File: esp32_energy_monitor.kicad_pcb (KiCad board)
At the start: 4 copper layers, 54 x 33.7 mm, 73 parts, among them IC1 CP2102N-A01-GQFN28, IC2 TPS63031DSKT, IC3 MCP73830T-2AAI_MYY, J1 USB, J2 Conn_01x03, J3 Conn_01x02, J4 Conn_01x02, J5 Conn_01x02, J6 Conn_01x04, J7 Conn_01x04, Q1 SS8050-G, Q2 SS8050-G, Q3 CSD16406Q3, Q4 CSD16406Q3, Q5 SS8050-G, SW1 SW_Push, SW2 SW_Push, U1 DRV8833PWPR, U2 BQ29700DSET

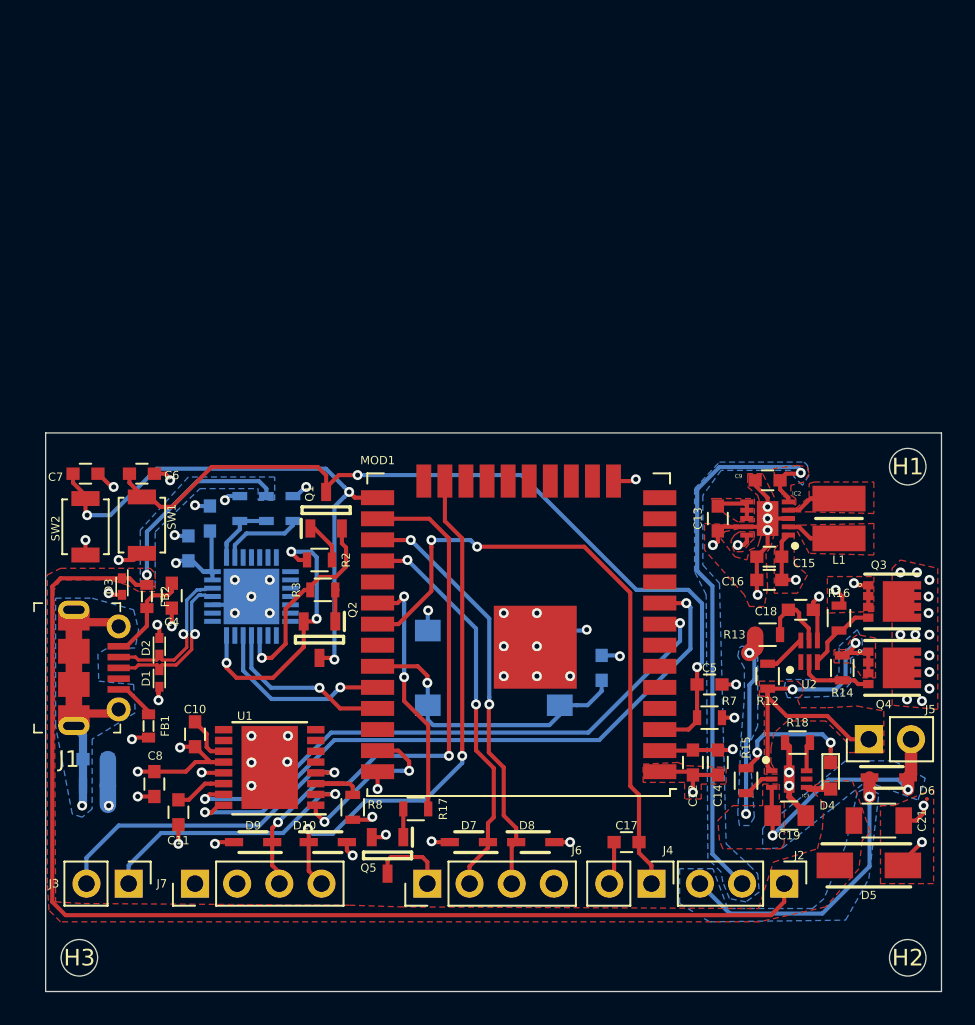
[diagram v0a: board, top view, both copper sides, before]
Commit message: Added the ADS1115IDGSR ADC circuit with the signal conditioning to current sensor SCT-013-020 (30A).
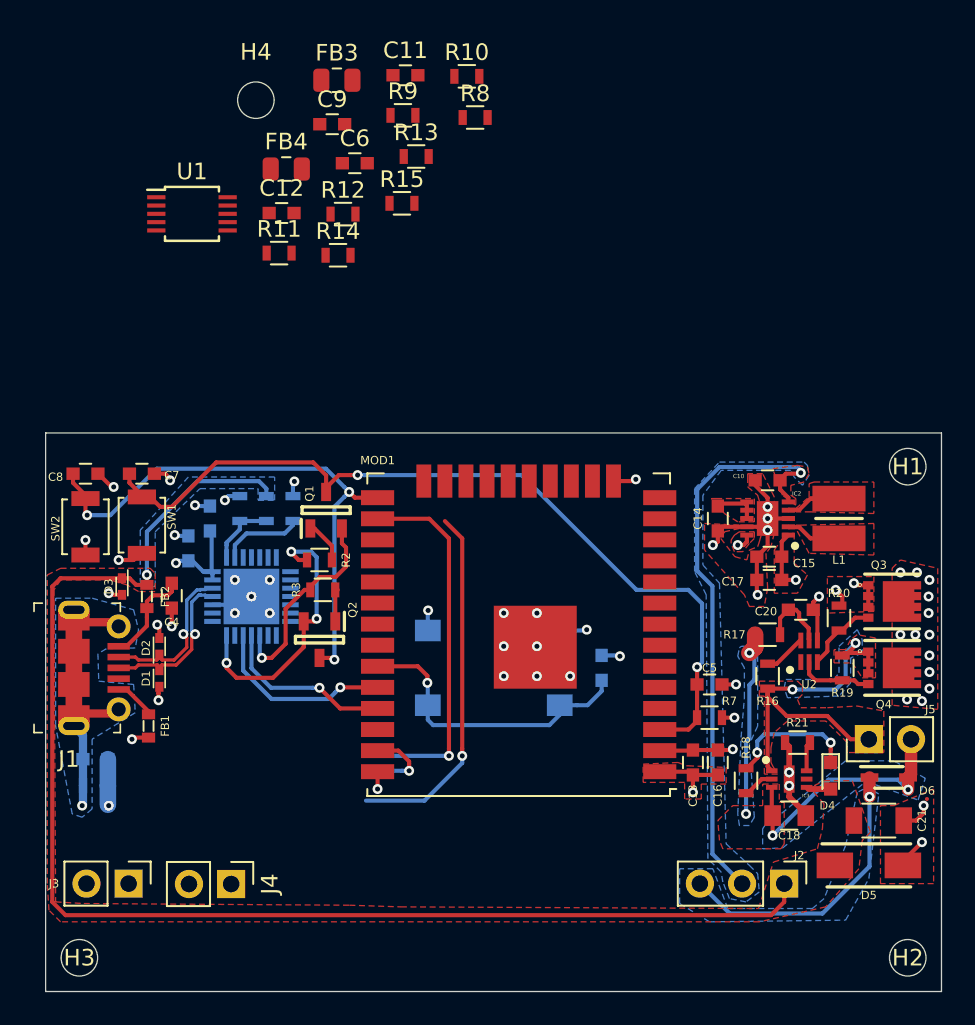
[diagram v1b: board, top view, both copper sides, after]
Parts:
- removed the C10 at (124.0, 91.5)
- removed the C17 at (150.0, 98.0)
- removed the C8 at (121.5, 94.5)
- removed D10, D7, D8, D9: PESD3V3L1BA,115, SamacSys_Parts:SOD2512X110N
- removed J6, J7: Conn_01x04, Pin_Headers:Pin_Header_Straight_1x04_Pitch2.54mm
- removed Q5: SS8050-G, SamacSys_Parts:SOT95P240X115-3N
- removed the R17 at (137.3, 96.0)
- added C12: 1uF, Capacitors_SMD:C_0603, F.Cu at (129.2, 60.1)
- added C6: 10uF ou 100uF, Capacitors_SMD:C_0603, F.Cu at (133.6, 57.1)
- added C9: 10uF ou 100uF, Capacitors_SMD:C_0603, F.Cu at (132.3, 54.7)
- added FB3: MMZ2012Y152BT000, Inductor_SMD:L_0805_2012Metric, F.Cu at (132.5, 52.1)
- added FB4: MMZ2012Y152BT000, Inductor_SMD:L_0805_2012Metric, F.Cu at (129.5, 57.4)
- added H4: M2Hole, Mounting_Holes:MountingHole_2.2mm_M2_DIN965, F.Cu at (127.7, 53.3)
- added R10: 100K/1%, Resistors_SMD:R_0603, F.Cu at (140.4, 51.9)
- added R11: 100K/1%, Resistors_SMD:R_0603, F.Cu at (129.1, 62.5)
- added R12: 10k, Resistors_SMD:R_0603, F.Cu at (132.9, 60.2)
- added R13: 10k, Resistors_SMD:R_0603, F.Cu at (137.3, 56.7)
- added R14: 10k, Resistors_SMD:R_0603, F.Cu at (132.6, 62.6)
- added R15: 10k, Resistors_SMD:R_0603, F.Cu at (136.5, 59.5)
- added R9: 100K/1%, Resistors_SMD:R_0603, F.Cu at (136.5, 54.2)
- C11: value 2.2uF -> 1uF
- J1: value USB -> USB_OTG
- R8: value 0.2R -> 100K/1%
- U1: value DRV8833PWPR -> ADS1115IDGS; footprint Housings_SSOP:HTSSOP-16-1EP_4.4x5mm_Pitch0.65mm -> Package_SO:TSSOP-10_3x3mm_P0.5mm
- moved C11 46.5 mm to (136.7, 51.8), turned to 0 degrees
- moved R8 42.2 mm to (140.9, 54.3), turned to 0 degrees
- moved U1 33.7 mm to (123.8, 60.1), turned to 0 degrees
- moved J4 25.3 mm to (126.2, 100.5)
- renumbered C9 to C10, C12 to C13, C13 to C14, C14 to C16, C16 to C17, C19 to C18, C20 to C19, C18 to C20, C6 to C7, C7 to C8, R12 to R16, R13 to R17, R15 to R18, R14 to R19, R16 to R20, R18 to R21
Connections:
- C11 pad 1: Net-(C11-Pad1) -> GNDD
- C11 pad 2: GND -> +3.3VADC
- IC1 pad 1: Net-(IC1-Pad1) -> (no net)
- IC1 pad 10: Net-(IC1-Pad10) -> (no net)
- IC1 pad 11: Net-(IC1-Pad11) -> (no net)
- IC1 pad 12: Net-(IC1-Pad12) -> (no net)
- IC1 pad 13: Net-(IC1-Pad13) -> (no net)
- IC1 pad 14: Net-(IC1-Pad14) -> (no net)
- IC1 pad 15: Net-(IC1-Pad15) -> (no net)
- IC1 pad 16: Net-(IC1-Pad16) -> (no net)
- IC1 pad 17: Net-(IC1-Pad17) -> (no net)
- IC1 pad 18: Net-(IC1-Pad18) -> (no net)
- IC1 pad 19: Net-(IC1-Pad19) -> (no net)
- IC1 pad 2: Net-(IC1-Pad2) -> (no net)
- IC1 pad 20: Net-(IC1-Pad20) -> (no net)
- IC1 pad 21: Net-(IC1-Pad21) -> (no net)
- IC1 pad 22: Net-(IC1-Pad22) -> (no net)
- IC1 pad 23: Net-(IC1-Pad23) -> (no net)
- IC1 pad 27: Net-(IC1-Pad27) -> (no net)
- IC3 pad 5: Net-(IC3-Pad5) -> (no net)
- J1 pad 4: Net-(J1-Pad4) -> (no net)
- J1 pad SH: GNDD -> (no net)
- J3 pad 2: Net-(J3-Pad2) -> Net-(C6-Pad1)
- J4 pad 1: IO19 -> Net-(J4-Pad1)
- J4 pad 2: GND -> Net-(C9-Pad1)
- MOD1 pad 10: R -> (no net)
- MOD1 pad 11: B -> (no net)
- MOD1 pad 12: G -> (no net)
- MOD1 pad 13: Net-(MOD1-Pad13) -> (no net)
- MOD1 pad 14: Net-(MOD1-Pad14) -> (no net)
- MOD1 pad 16: Net-(MOD1-Pad16) -> (no net)
- MOD1 pad 17: Net-(MOD1-Pad17) -> (no net)
- MOD1 pad 18: Net-(MOD1-Pad18) -> (no net)
- MOD1 pad 19: Net-(MOD1-Pad19) -> (no net)
- MOD1 pad 20: Net-(MOD1-Pad20) -> (no net)
- MOD1 pad 21: Net-(MOD1-Pad21) -> (no net)
- MOD1 pad 22: Net-(MOD1-Pad22) -> (no net)
- MOD1 pad 23: NFC_RX -> (no net)
- MOD1 pad 24: Net-(MOD1-Pad24) -> (no net)
- MOD1 pad 26: NFC_TX -> (no net)
- MOD1 pad 27: FINGER_TX -> (no net)
- MOD1 pad 28: FINGER_RX -> (no net)
- MOD1 pad 29: Net-(MOD1-Pad29) -> (no net)
- MOD1 pad 30: FINGER_EN -> (no net)
- MOD1 pad 31: IO19 -> (no net)
- MOD1 pad 32: Net-(MOD1-Pad32) -> (no net)
- MOD1 pad 36: Net-(MOD1-Pad36) -> (no net)
- MOD1 pad 37: IO23 -> (no net)
- MOD1 pad 4: Net-(MOD1-Pad4) -> (no net)
- MOD1 pad 5: Net-(MOD1-Pad5) -> (no net)
- MOD1 pad 6: Net-(MOD1-Pad6) -> (no net)
- MOD1 pad 7: Net-(MOD1-Pad7) -> (no net)
- MOD1 pad 8: IO32 -> (no net)
- MOD1 pad 9: IO33 -> (no net)
- R8 pad 1: Net-(R8-Pad1) -> Net-(C6-Pad1)
- R8 pad 2: GND -> +3.3VADC
- U1 pad 1: IO23 -> Net-(R13-Pad2)
- U1 pad 10: Net-(U1-Pad10) -> SCL-ADS
- U1 pad 2: Net-(J3-Pad1) -> ALERT-ADS
- U1 pad 3: Net-(R8-Pad1) -> GNDD
- U1 pad 4: Net-(J3-Pad2) -> Net-(J3-Pad1)
- U1 pad 5: Net-(U1-Pad5) -> Net-(J4-Pad1)
- U1 pad 6: Net-(U1-Pad6) -> (no net)
- U1 pad 7: Net-(U1-Pad7) -> (no net)
- U1 pad 8: Net-(U1-Pad8) -> +3.3VADC
- U1 pad 9: Net-(U1-Pad9) -> SDA-ADS
- U2 pad 1: Net-(U2-Pad1) -> (no net)
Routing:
- net IO33: track 39.1 -> 0.00 mm, vias 2 -> 0
- net IO19: track 38.5 -> 0.00 mm, vias 2 -> 0
- net IO32: track 36.1 -> 0.00 mm, vias 2 -> 0
- net NFC_TX: track 33.9 -> 0.00 mm, vias 2 -> 0
- net (no net): track 0.00 -> 27.1 mm, vias 0 -> 2
- net FINGER_TX: track 25.5 -> 0.00 mm, vias 2 -> 0
- net FINGER_RX: track 24.1 -> 0.00 mm, vias 2 -> 0
- net Net-(J3-Pad2): track 19.8 -> 0.00 mm, vias 1 -> 0
- net Net-(J3-Pad1): track 16.5 -> 0.00 mm, vias 1 -> 0
- net FINGER_EN: track 15.2 -> 0.00 mm, vias 2 -> 0
- net GND: track 68.2 -> 55.6 mm, vias 58 -> 44
- net NFC_RX: track 32.2 -> 21.7 mm, vias 2 -> 1
- net IO23: track 10.3 -> 0.00 mm, vias 2 -> 0
- net +3V3: track 25.1 -> 16.5 mm, vias 8 -> 6
- net Net-(J6-Pad1): track 4.85 -> 0.00 mm
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- added copper zone on B.Cu, net Net-(C9-Pad1)
- added copper zone on F.Cu, net Net-(C9-Pad1)
- removed copper zone on B.Cu, net Net-(C10-Pad1)
- removed copper zone on F.Cu, net Net-(C10-Pad1)
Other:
- board text added: "CT 01"
- board text added: "CT 02"
- board text removed: "FINGER"
- board text removed: "MOTOR"
- board text removed: "NFC"
- board text removed: "uSwitch"

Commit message: Schematic: Removed ADS1115 circuit. Removed Battery Protection circuit. Removed Battery Charger circuit. Removed Wake Up Button. Added external access circuit. Added three current measure circuit. It will be powered with power supply micro-usb only.
Layout:
Added the footprint library of the project.
Changed the ESP32 footprint.
Changed the position of the power supply circuit. (near of USB connector)

3D View:
Added ESP32 3D format step.
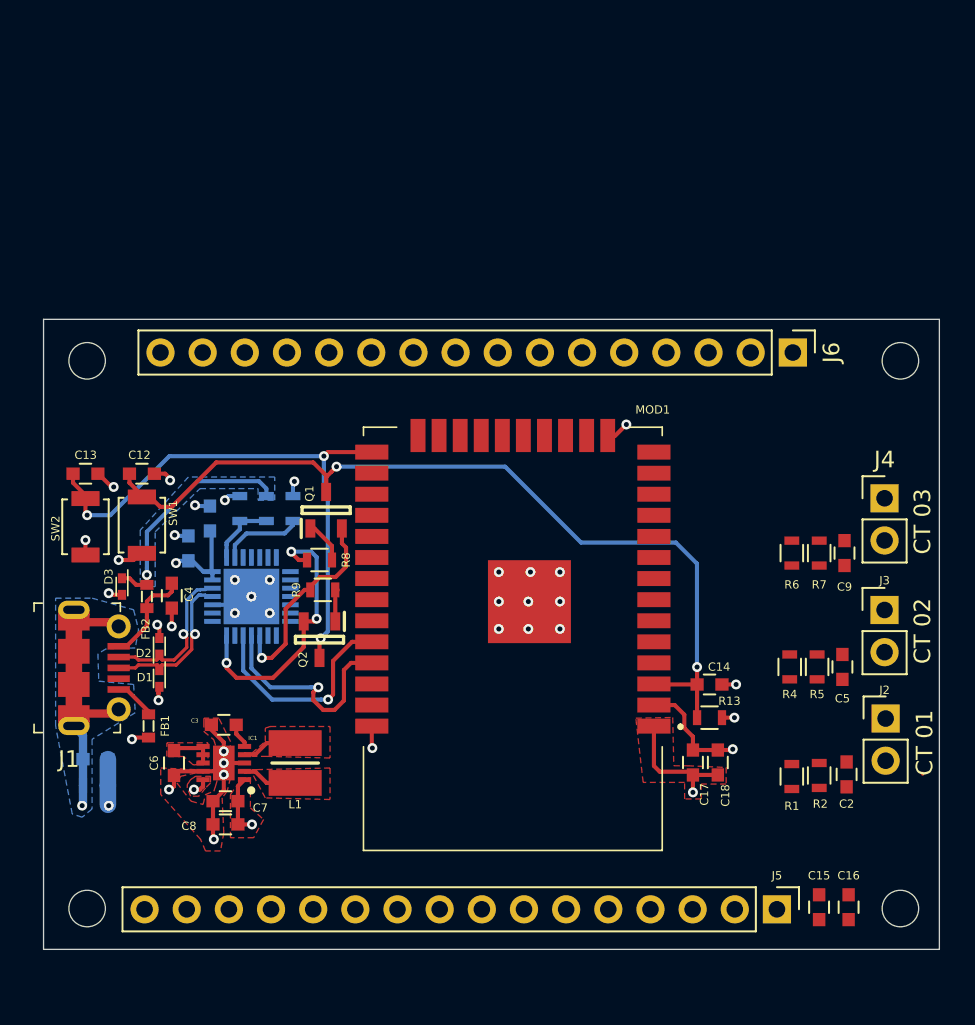
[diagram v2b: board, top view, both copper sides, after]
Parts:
- removed C19, C20: 0.1uF, Capacitors_SMD:C_0603
- removed C21: 4.7uF 25V/XR7, Capacitors_SMD:C_1206
- removed D4: LED, LEDs:LED_0603
- removed D5: SMAJ5.0A, SamacSys_Parts:DIOM5026X229N
- removed D6: BAT760-7, SamacSys_Parts:SOD2513X120N
- removed FB3, FB4: MMZ2012Y152BT000, Inductor_SMD:L_0805_2012Metric
- removed IC3: MCP73830T-2AAI_MYY, SamacSys_Parts:SON50P200X200X80-7N-D
- removed Q3, Q4: CSD16406Q3, SamacSys_Parts:DQG_VSON-CLIP
- removed R14, R15: 10k, Resistors_SMD:R_0603
- removed R16: 2.2k, Resistors_SMD:R_0603
- removed R17: 330R, Resistors_SMD:R_0603
- removed R18: 1k, Resistors_SMD:R_0603
- removed R19, R20: 5M, Resistors_SMD:R_0603
- removed R21: 1.5k, Resistors_SMD:R_0603
- removed S1: PTS645SM43SMTR92_LFS, digikey-footprints:Switch_Tactile_SMD_6x6mm_PTS645
- removed U1: ADS1115IDGS, Package_SO:TSSOP-10_3x3mm_P0.5mm
- removed U2: BQ29700DSET, SamacSys_Parts:SON50P150X150X80-6N
- added J6: Conn_01x16, Connector_PinHeader_2.54mm:PinHeader_1x16_P2.54mm_Vertical, F.Cu at (160.0, 68.5)
- C1: value 4.7uF/6.3V -> 0.1uF; footprint Capacitors_SMD:C_0603 -> proj_kicad_esp32_energy_consumption:C_0603
- C10: value 10uF 6.3V X7R -> 4.7uF/6.3V; footprint Capacitors_SMD:C_0603 -> proj_kicad_esp32_energy_consumption:C_0603; moved to B.Cu
- C11: value 1uF -> 0.1uF; footprint Capacitors_SMD:C_0603 -> proj_kicad_esp32_energy_consumption:C_0603; moved to B.Cu
- C12: value 1uF -> 0.1uF; footprint Capacitors_SMD:C_0603 -> proj_kicad_esp32_energy_consumption:C_0603
- C13, C16, C4, C9: footprint Capacitors_SMD:C_0603 -> proj_kicad_esp32_energy_consumption:C_0603
- C14: value 0.1uF XR7 ceramic -> 0.1uF; footprint Capacitors_SMD:C_0603 -> proj_kicad_esp32_energy_consumption:C_0603
- C15, C17: value 10uF -> 0.1uF; footprint Capacitors_SMD:C_0603 -> proj_kicad_esp32_energy_consumption:C_0603
- C18: value 4.7uF 16V/XR7 -> 10uF; footprint Capacitors_SMD:C_0805 -> proj_kicad_esp32_energy_consumption:C_0603
- C2: value 0.1uF -> 10uF ou 100uF; footprint Capacitors_SMD:C_0603 -> proj_kicad_esp32_energy_consumption:C_0603; moved to F.Cu
- C3: value 0.1uF -> 10uF 6.3V X7R; footprint Capacitors_SMD:C_0603 -> proj_kicad_esp32_energy_consumption:C_0603; moved to F.Cu
- C5: value 0.1uF -> 10uF ou 100uF; footprint Capacitors_SMD:C_0603 -> proj_kicad_esp32_energy_consumption:C_0603
- C6: value 10uF ou 100uF -> 0.1uF XR7 ceramic; footprint Capacitors_SMD:C_0603 -> proj_kicad_esp32_energy_consumption:C_0603
- C7, C8: value 0.1uF -> 10uF; footprint Capacitors_SMD:C_0603 -> proj_kicad_esp32_energy_consumption:C_0603
- D1, D2, D3: footprint padlock.pretty:DPY_R-PX1SON-N2_ -> proj_kicad_esp32_energy_consumption:DPY_R-PX1SON-N2_
- FB1, FB2: footprint digikey-footprints:0603 -> proj_kicad_esp32_energy_consumption:0603
- H1, H2, H3, H4: footprint Mounting_Holes:MountingHole_2.2mm_M2_DIN965 -> proj_kicad_esp32_energy_consumption:MountingHole_2.2mm_M2_DIN965
- IC1: value CP2102N-A01-GQFN28 -> TPS63031DSKT; footprint SamacSys_Parts:QFN50P500X500X80-29N-D -> proj_kicad_esp32_energy_consumption:SON50P250X250X80-11N-D; moved to F.Cu
- IC2: value TPS63031DSKT -> CP2102N-A01-GQFN28; footprint SamacSys_Parts:SON50P250X250X80-11N-D -> proj_kicad_esp32_energy_consumption:QFN50P500X500X80-29N-D; moved to B.Cu
- J1: footprint digikey-footprints:USB_Micro_B_Female_1050170001 -> proj_kicad_esp32_energy_consumption:USB_Micro_B_Female_1050170001
- J2: value Conn_01x03 -> Conn_01x02; footprint Pin_Headers:Pin_Header_Straight_1x03_Pitch2.54mm -> proj_kicad_esp32_energy_consumption:Pin_Header_Straight_1x02_Pitch2.54mm
- J3, J4: footprint Pin_Headers:Pin_Header_Straight_1x02_Pitch2.54mm -> proj_kicad_esp32_energy_consumption:Pin_Header_Straight_1x02_Pitch2.54mm
- J5: value Conn_01x02 -> Conn_01x16; footprint Pin_Headers:Pin_Header_Straight_1x02_Pitch2.54mm -> Connector_PinHeader_2.54mm:PinHeader_1x16_P2.54mm_Vertical
- L1: footprint SamacSys_Parts:INDC3030X120N -> proj_kicad_esp32_energy_consumption:INDC3030X120N
- MOD1: footprint padlock.pretty:ESP32-WROOM-32U -> ESP32-WROOM-32D:ESP32WROOM32D
- Q1, Q2: footprint SamacSys_Parts:SOT95P240X115-3N -> proj_kicad_esp32_energy_consumption:SOT95P240X115-3N
- R1: value 330R -> 100K/1%; footprint Resistors_SMD:R_0603 -> proj_kicad_esp32_energy_consumption:R_0603; moved to F.Cu
- R10: value 100K/1% -> 22.1k; footprint Resistors_SMD:R_0603 -> proj_kicad_esp32_energy_consumption:R_0603; moved to B.Cu
- R11: value 100K/1% -> 47.5k; footprint Resistors_SMD:R_0603 -> proj_kicad_esp32_energy_consumption:R_0603; moved to B.Cu
- R12: value 10k -> 1k; footprint Resistors_SMD:R_0603 -> proj_kicad_esp32_energy_consumption:R_0603; moved to B.Cu
- R13: footprint Resistors_SMD:R_0603 -> proj_kicad_esp32_energy_consumption:R_0603
- R2, R7: value 10k -> 100K/1%; footprint Resistors_SMD:R_0603 -> proj_kicad_esp32_energy_consumption:R_0603
- R3: value 10k -> 330R; footprint Resistors_SMD:R_0603 -> proj_kicad_esp32_energy_consumption:R_0603; moved to B.Cu
- R4: value 22.1k -> 100K/1%; footprint Resistors_SMD:R_0603 -> proj_kicad_esp32_energy_consumption:R_0603; moved to F.Cu
- R5: value 47.5k -> 100K/1%; footprint Resistors_SMD:R_0603 -> proj_kicad_esp32_energy_consumption:R_0603; moved to F.Cu
- R6: value 1k -> 100K/1%; footprint Resistors_SMD:R_0603 -> proj_kicad_esp32_energy_consumption:R_0603; moved to F.Cu
- R8, R9: value 100K/1% -> 10k; footprint Resistors_SMD:R_0603 -> proj_kicad_esp32_energy_consumption:R_0603
- SW1, SW2: footprint Buttons_Switches_SMD:SW_SPST_B3U-1000P -> proj_kicad_esp32_energy_consumption:SW_SPST_B3U-1000P
- moved H2 61.1 mm to (117.5, 69.0)
- moved J3 48.4 mm to (165.5, 84.0), turned to 0 degrees
- moved J4 45.7 mm to (165.5, 77.3), turned to 0 degrees
- moved C2 45.3 mm to (163.3, 93.9), turned to 270 degrees
- moved R1 42.0 mm to (160.0, 94.0), turned to 270 degrees
- moved H4 41.9 mm to (166.5, 69.0)
- moved C13 40.5 mm to (117.4, 75.8), turned to 180 degrees
- moved C9 40.3 mm to (163.1, 80.6), turned to 270 degrees
- moved R13 38.2 mm to (155.0, 90.5), turned to 180 degrees
- moved C6 37.7 mm to (122.7, 93.2), turned to 270 degrees
- moved R5 36.1 mm to (161.5, 87.4), turned to 90 degrees
- moved L1 35.9 mm to (130.0, 93.2)
- moved C10 33.7 mm to (124.9, 78.5), turned to 90 degrees
- moved R4 32.9 mm to (159.8, 87.4), turned to 270 degrees
- moved R2 32.8 mm to (161.6, 94.0), turned to 90 degrees
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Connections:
- C1 pad 1: +3V3 -> GND
- C1 pad 2: GND -> GNDD
- C10 pad 1: Net-(C10-Pad1) -> +3V3
- C11 pad 1: GNDD -> +3V3
- C11 pad 2: +3.3VADC -> GND
- C12 pad 1: +3V3 -> GND
- C12 pad 2: GND -> EN
- C13 pad 1: +3V3 -> GND
- C13 pad 2: GND -> IO0
- C14 pad 1: Net-(C14-Pad1) -> EN
- C18 pad 1: VBAT_+ -> +3V3
- C2 pad 1: GND -> Net-(C2-Pad1)
- C2 pad 2: GNDD -> GND
- C3 pad 1: +3V3 -> VBUS
- C5 pad 1: EN -> Net-(C5-Pad1)
- C6 pad 2: GNDD -> GND
- C7 pad 1: GND -> +3V3
- C7 pad 2: EN -> GND
- C8 pad 1: GND -> +3V3
- C8 pad 2: IO0 -> GND
- C9 pad 2: GNDD -> GND
- IC1 pad 1: (no net) -> +3V3
- IC1 pad 10: (no net) -> +3V3
- IC1 pad 11: (no net) -> GND
- IC1 pad 2: (no net) -> Net-(IC1-Pad2)
- IC1 pad 4: USB_DP -> Net-(IC1-Pad4)
- IC1 pad 5: USB_DN -> VBUS
- IC1 pad 6: +3V3 -> Net-(C6-Pad1)
- IC1 pad 7: +3V3 -> Net-(C6-Pad1)
- IC1 pad 8: Net-(IC1-Pad8) -> Net-(C6-Pad1)
- IC1 pad 9: Net-(IC1-Pad9) -> GND
- IC2 pad 1: +3V3 -> (no net)
- IC2 pad 10: +3V3 -> (no net)
- IC2 pad 11: GND -> (no net)
- IC2 pad 4: Net-(IC2-Pad4) -> USB_DP
- IC2 pad 5: Net-(C10-Pad1) -> USB_DN
- IC2 pad 6: Net-(C14-Pad1) -> +3V3
- IC2 pad 7: Net-(C14-Pad1) -> +3V3
- IC2 pad 8: Net-(C14-Pad1) -> Net-(IC2-Pad8)
- IC2 pad 9: GND -> Net-(IC2-Pad9)
- J2 pad 1: VBUS -> ADC1_6
- J2 pad 2: Net-(C10-Pad1) -> Net-(C2-Pad1)
- J3 pad 1: Net-(J3-Pad1) -> ADC1_7
- J3 pad 2: Net-(C6-Pad1) -> Net-(C5-Pad1)
- J4 pad 1: Net-(J4-Pad1) -> ADC1_4
- J5 pad 1: VBAT_- -> +3V3
- J5 pad 2: VBAT_+ -> IO25
- L1 pad 1: Net-(IC2-Pad2) -> Net-(IC1-Pad2)
- L1 pad 2: Net-(IC2-Pad4) -> Net-(IC1-Pad4)
- MOD1 pad 10: (no net) -> IO25
- MOD1 pad 11: (no net) -> IO26
- MOD1 pad 12: (no net) -> IO27
- MOD1 pad 13: (no net) -> IO14
- MOD1 pad 14: (no net) -> IO12
- MOD1 pad 16: (no net) -> IO13
- MOD1 pad 17: (no net) -> SD2
- MOD1 pad 18: (no net) -> SD3
- MOD1 pad 19: (no net) -> SCS
- MOD1 pad 20: (no net) -> CLK
- MOD1 pad 21: (no net) -> SD0
- MOD1 pad 22: (no net) -> SD1
- MOD1 pad 23: (no net) -> IO15
- MOD1 pad 24: (no net) -> IO2
- MOD1 pad 26: (no net) -> IO4
- MOD1 pad 27: (no net) -> IO16
- MOD1 pad 28: (no net) -> IO17
- MOD1 pad 29: (no net) -> IO5
- MOD1 pad 30: (no net) -> IO18
- MOD1 pad 31: (no net) -> IO19
- MOD1 pad 36: (no net) -> IO22
- MOD1 pad 37: (no net) -> IO23
- MOD1 pad 4: (no net) -> SENSOR_VP
- MOD1 pad 5: (no net) -> SENSOR_VN
- MOD1 pad 6: (no net) -> ADC1_6
- MOD1 pad 7: (no net) -> ADC1_7
- MOD1 pad 8: (no net) -> ADC1_4
- MOD1 pad 9: (no net) -> IO33
- R1 pad 1: GND -> Net-(C2-Pad1)
- R1 pad 2: GNDD -> +3V3
- R10 pad 1: Net-(C9-Pad1) -> Net-(IC2-Pad8)
- R10 pad 2: +3.3VADC -> VBUS
- R11 pad 1: GNDD -> GND
- R11 pad 2: Net-(C9-Pad1) -> Net-(IC2-Pad8)
- R12 pad 1: ALERT-ADS -> +3V3
- R12 pad 2: +3.3VADC -> Net-(IC2-Pad9)
- R13 pad 1: GNDD -> +3V3
- R13 pad 2: Net-(R13-Pad2) -> EN
- R2 pad 1: Net-(Q1-Pad1) -> GND
- R2 pad 2: DTR -> Net-(C2-Pad1)
- R3 pad 1: Net-(Q2-Pad1) -> GND
- R3 pad 2: RTS -> GNDD
- R4 pad 1: Net-(IC1-Pad8) -> Net-(C5-Pad1)
- R4 pad 2: VBUS -> +3V3
- R5 pad 2: Net-(IC1-Pad8) -> Net-(C5-Pad1)
- R6 pad 1: +3V3 -> Net-(C9-Pad1)
- R6 pad 2: Net-(IC1-Pad9) -> +3V3
- R7 pad 1: +3V3 -> GND
- R7 pad 2: EN -> Net-(C9-Pad1)
- R8 pad 1: Net-(C6-Pad1) -> Net-(Q1-Pad1)
- R8 pad 2: +3.3VADC -> DTR
- R9 pad 1: GNDD -> Net-(Q2-Pad1)
- R9 pad 2: Net-(C6-Pad1) -> RTS
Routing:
- net VBUS: track 84.8 -> 15.5 mm
- net Net-(C10-Pad1): track 34.9 -> 0.00 mm, vias 1 -> 0
- net VBAT_+: track 27.2 -> 0.00 mm, vias 4 -> 0
- net (no net): track 27.1 -> 0.00 mm, vias 2 -> 0
- net VBAT_-: track 24.3 -> 0.00 mm, vias 2 -> 0
- net NFC_RX: track 21.7 -> 0.00 mm, vias 1 -> 0
- net IO21: track 18.3 -> 0.00 mm, vias 1 -> 0
- net VBAT: track 17.6 -> 0.00 mm, vias 1 -> 0
- net GND: track 55.6 -> 39.7 mm, vias 44 -> 36
- net Net-(D4-Pad1): track 8.25 -> 0.00 mm, vias 2 -> 0
- net Net-(IC2-Pad9): track 0.00 -> 5.00 mm
- net Net-(IC1-Pad9): track 5.00 -> 0.00 mm
- net Net-(Q4-Pad4): track 4.54 -> 0.00 mm
- net Net-(Q3-Pad4): track 4.52 -> 0.00 mm
- net Net-(C20-Pad2): track 4.34 -> 0.00 mm
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- added copper zone on F.Cu, net Net-(C6-Pad1)
- removed copper zone on F.Cu, net Net-(C14-Pad1)
- removed copper zone on B.Cu, net Net-(C9-Pad1)
- removed copper zone on F.Cu, net Net-(C9-Pad1)
- removed copper zone on F.Cu, net Net-(Q3-Pad5)
- removed copper zone on B.Cu, net VBAT
- removed copper zone on B.Cu, net VBAT_+
- removed copper zone on F.Cu, net VBAT_+
- removed copper zone on B.Cu, net VBAT_-
- removed copper zone on F.Cu, net VBAT_-
- removed copper zone on F.Cu, net VBUS
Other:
- board size 54 x 33.7 mm -> 54 x 38 mm
- board text added: "CT 03"
- board text removed: "+"
- board text removed: "+3V3"
- board text removed: "-"
- board text removed: "AOUT1"
- board text removed: "AOUT2"
- board text removed: "BAT"
- board text removed: "C"
- board text removed: "CHAVE"
- board text removed: "F_RX"
- board text removed: "F_TX"
- board text removed: "GND"
- board text removed: "IO19"
- board text removed: "N_RX"
- board text removed: "N_TX"
- board text removed: "VBAT"
- board text removed: "VBUS"

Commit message: Added to the library of the project the pin header footprint. Added the first version of the Bill of the Materials (BoM) of the board. Added the StackUp of the board.
Schematic:
Changed the position of the pins on J5 and J6 to layout better on the board.

Layout:
Added all the route tracks of the J5 and J6 connectors
Added 3V3 Power Plane and the VBUS Power Plane
Changed the format of the Ground Plane.
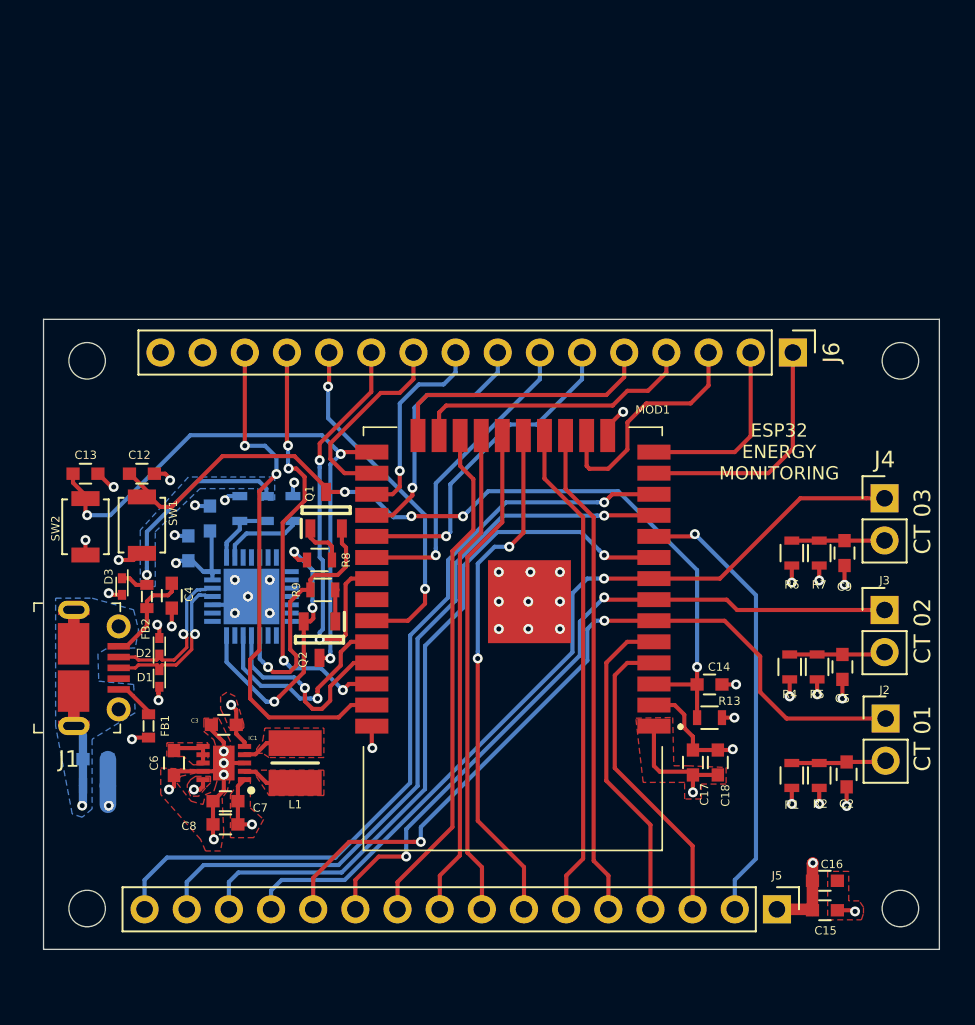
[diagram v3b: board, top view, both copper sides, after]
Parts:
- moved C16 2.14 mm to (162.0, 100.3), turned to 0 degrees
- moved C15 0.40 mm to (162.0, 102.1), turned to 0 degrees
- moved R1 0.06 mm to (160.0, 94.0)
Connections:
- IC2 pad 2: Net-(IC2-Pad2) -> (no net)
- J1 pad SH: (no net) -> GNDD
- J5 pad 13: IO33 -> ADC1_4
- J5 pad 14: ADC1_4 -> IO33
- J6 pad 1: IO2 -> IO14
- J6 pad 10: IO18 -> IO4
- J6 pad 2: IO4 -> IO12
- J6 pad 3: IO5 -> IO13
- J6 pad 4: IO12 -> IO15
- J6 pad 5: IO13 -> IO2
- J6 pad 6: IO14 -> IO5
- J6 pad 7: IO15 -> IO18
- J6 pad 8: IO16 -> IO17
- J6 pad 9: IO17 -> IO16
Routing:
- net ADC1_4: track 0.00 -> 50.0 mm, vias 0 -> 1
- net IO27: track 0.00 -> 48.6 mm, vias 0 -> 1
- net ADC1_6: track 0.00 -> 48.1 mm, vias 0 -> 2
- net IO26: track 0.00 -> 45.5 mm, vias 0 -> 1
- net ADC1_7: track 0.00 -> 43.2 mm, vias 0 -> 2
- net IO33: track 0.00 -> 43.1 mm, vias 0 -> 1
- net SCS: track 0.00 -> 31.4 mm, vias 0 -> 2
- net IO23: track 0.00 -> 31.1 mm, vias 0 -> 2
- net SD1: track 0.00 -> 30.8 mm
- net SD3: track 0.00 -> 29.9 mm
- net CLK: track 0.00 -> 29.8 mm
- net SD2: track 0.00 -> 29.6 mm
- net SD0: track 0.00 -> 29.6 mm
- net IO25: track 0.00 -> 27.2 mm, vias 0 -> 1
- net IO22: track 0.00 -> 26.0 mm, vias 0 -> 4
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- added copper zone on F.Cu, net Net-(IC1-Pad2)
- added copper zone on F.Cu, net Net-(IC1-Pad4)
- added copper zone on F.Cu, net VBUS
- added copper zone on Power_Plane, net VBUS
- removed copper zone on F.Cu, net Net-(IC2-Pad2)
- removed copper zone on F.Cu, net Net-(IC2-Pad4)
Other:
- board text added: "ESP32 ENERGY MONITORING"
